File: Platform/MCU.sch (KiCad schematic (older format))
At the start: 28 parts

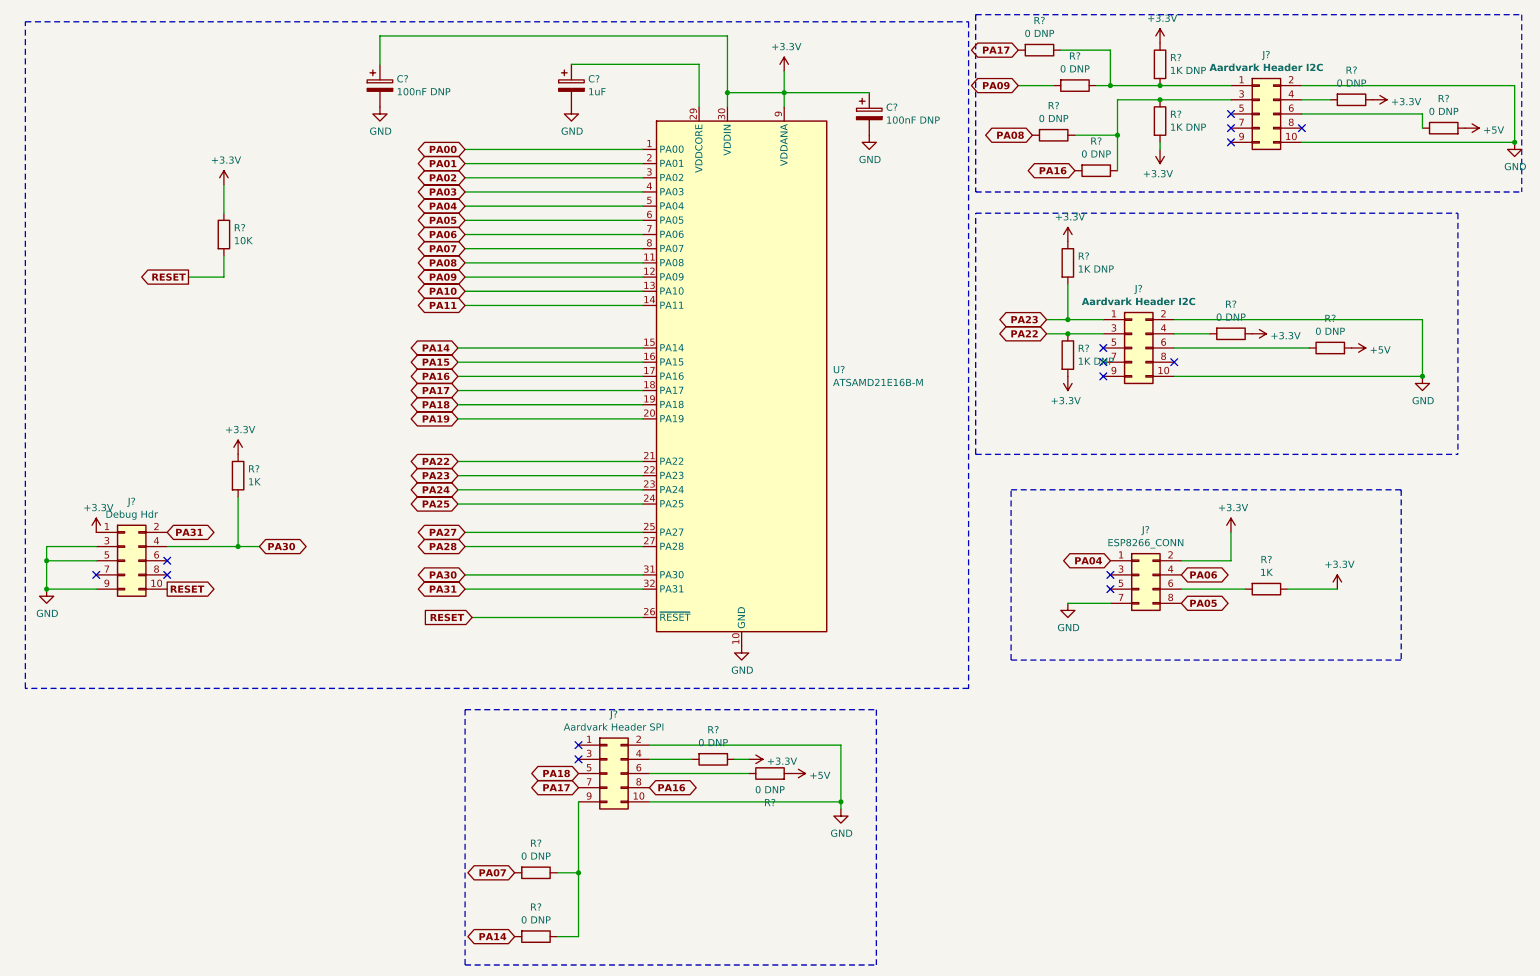
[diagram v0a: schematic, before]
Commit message: Added RTC and EEPROM
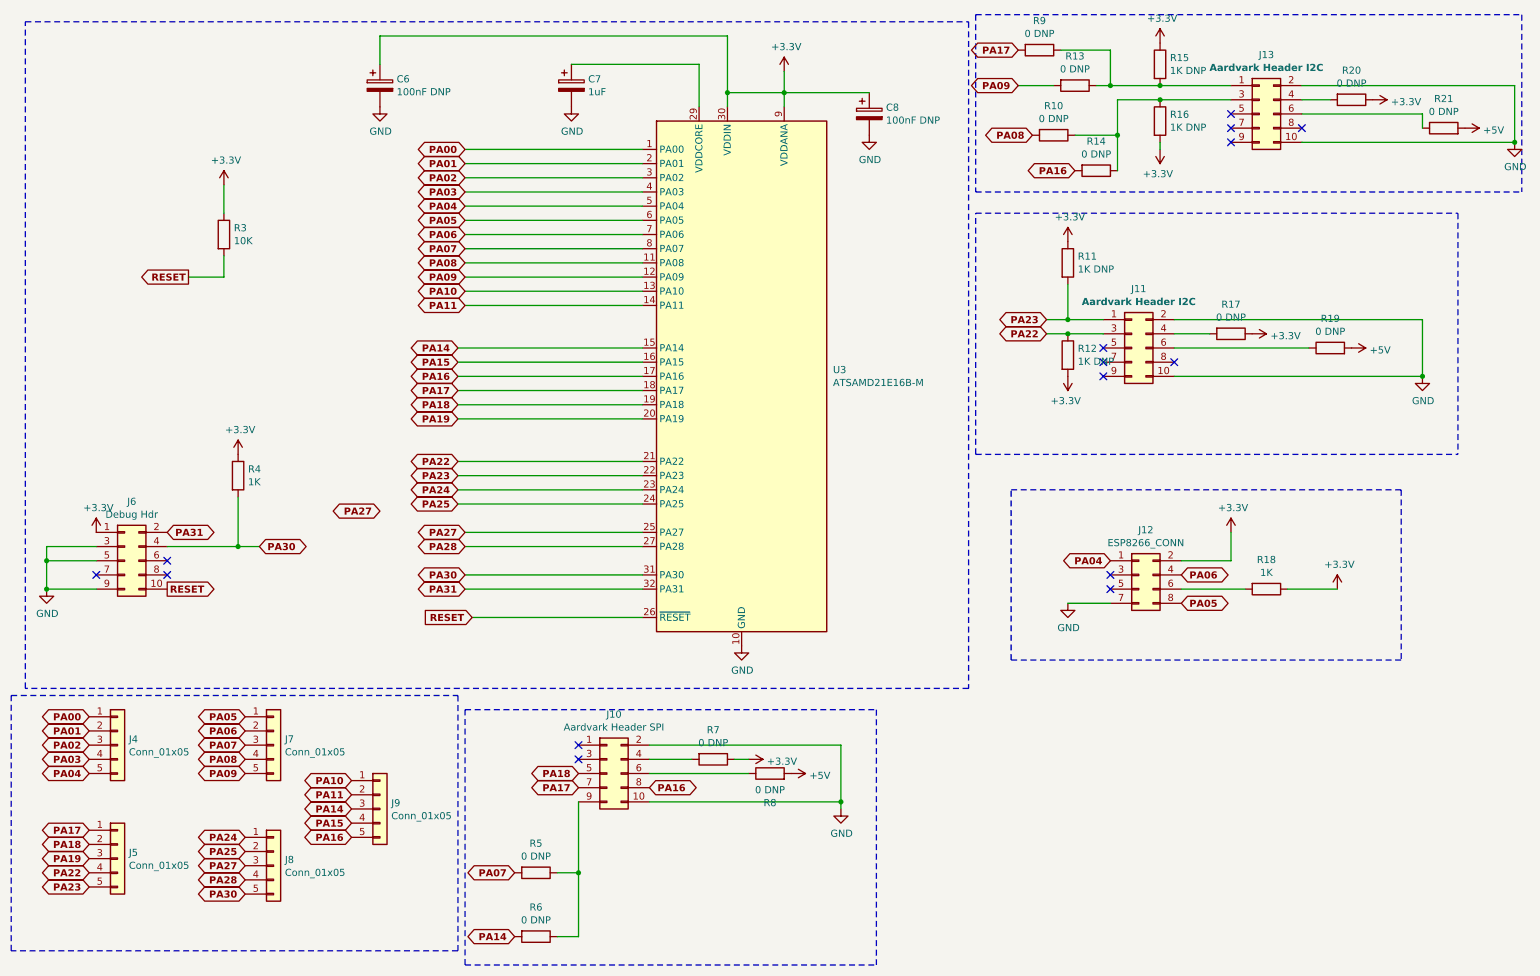
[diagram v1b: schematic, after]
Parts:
- added J4, J5, J7, J8, J9: Conn_01x05, symbol Connector_Generic:Conn_01x05
- gave numbers to parts that had none: 28
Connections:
- net PA00: now also J4.1 (Pin_1)
- net PA01: now also J4.2 (Pin_2)
- net PA02: now also J4.3 (Pin_3)
- net PA03: now also J4.4 (Pin_4)
- net PA04: now also J4.5 (Pin_5)
- net PA05: now also J7.1 (Pin_1)
- net PA06: now also J7.2 (Pin_2)
- net PA07: now also J7.3 (Pin_3)
- net PA08: now also J7.4 (Pin_4)
- net PA09: now also J7.5 (Pin_5)
- net PA10: now also J9.1 (Pin_1)
- net PA11: now also J9.2 (Pin_2)
- net PA14: now also J9.3 (Pin_3)
- net PA15: now also J9.4 (Pin_4)
- net PA16: now also J9.5 (Pin_5)
- net PA17: now also J5.1 (Pin_1)
- net PA18: now also J5.2 (Pin_2)
- net PA19: now also J5.3 (Pin_3)
- net PA22: now also J5.4 (Pin_4)
- net PA23: now also J5.5 (Pin_5)
- net PA24: now also J8.1 (Pin_1)
- net PA25: now also J8.2 (Pin_2)
- net PA27: now also J8.3 (Pin_3)
- net PA28: now also J8.4 (Pin_4)
- net PA30: now also J8.5 (Pin_5)

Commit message: changes
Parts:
- added J9: Conn_01x05, symbol Connector_Generic:Conn_01x05
- renumbered J9 to J10, J10 to J11, J11 to J12, J12 to J13, J13 to J14
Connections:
- net +3V3: now also J9.1 (Pin_1)
- net +5V: now also J9.5 (Pin_5)
- net GND: now also J9.2 (Pin_2), J9.3 (Pin_3), J9.4 (Pin_4)
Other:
- moved on the sheet: J10

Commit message: Fixed ERC errors.
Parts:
- U3: symbol MCU_Microchip_SAMD:ATSAMD21E16B-M -> Platform-rescue:ATSAMD21E16B-M-MCU_Microchip_SAMD
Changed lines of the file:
@@
 RESET
 $Comp
-L MCU_Microchip_SAMD:ATSAMD21E16B-M U3
+L Platform-rescue:ATSAMD21E16B-M-MCU_Microchip_SAMD U3
 U 1 1 5FAA26F4
 P 5700 3450

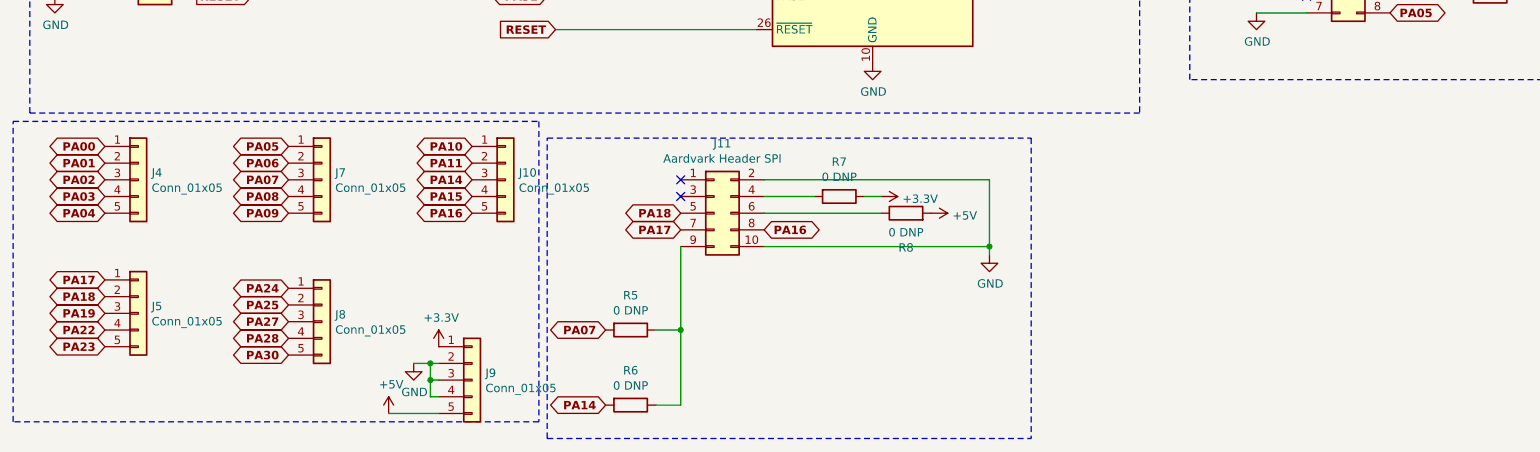
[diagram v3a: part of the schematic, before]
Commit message: added GPIO header for segment display.
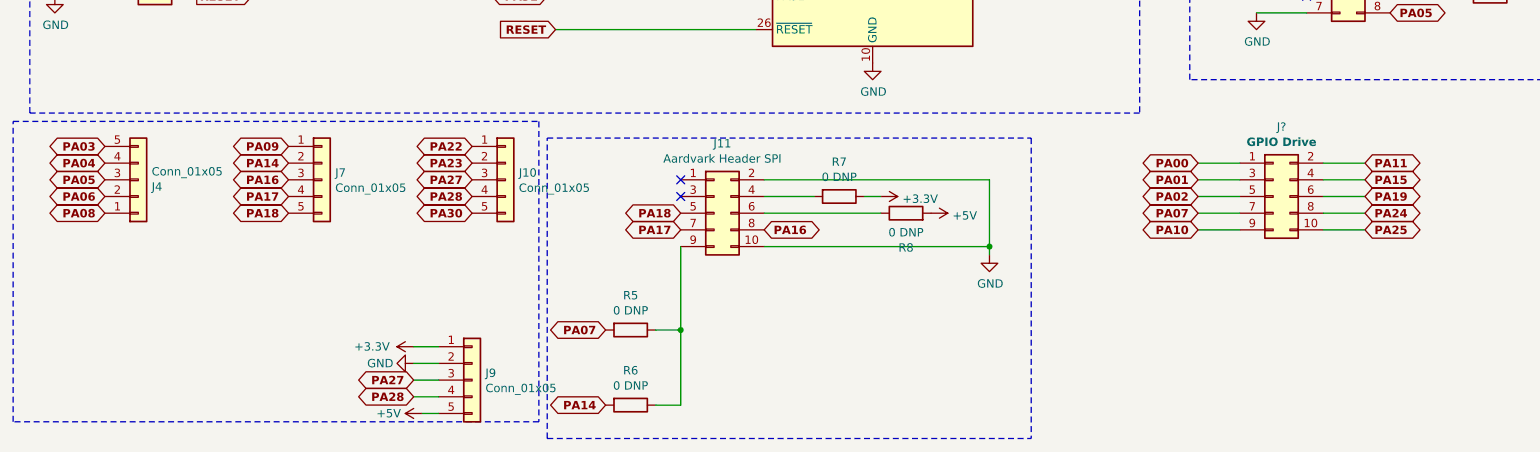
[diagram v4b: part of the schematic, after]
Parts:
- removed J5, J8: Conn_01x05, symbol Connector_Generic:Conn_01x05
- added J?: GPIO Drive, symbol Connector_Generic:Conn_02x05_Odd_Even
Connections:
- net GND: no longer J9.3 (Pin_3), J9.4 (Pin_4)
- net PA00: now also J?.1 (Pin_1); no longer J4.1 (Pin_1)
- net PA01: now also J?.3 (Pin_3); no longer J4.2 (Pin_2)
- net PA02: now also J?.5 (Pin_5); no longer J4.3 (Pin_3)
- net PA03: now also J4.5 (Pin_5); no longer J4.4 (Pin_4)
- net PA04: now also J4.4 (Pin_4); no longer J4.5 (Pin_5)
- net PA05: now also J4.3 (Pin_3); no longer J7.1 (Pin_1)
- net PA06: now also J4.2 (Pin_2); no longer J7.2 (Pin_2)
- net PA07: now also J?.7 (Pin_7); no longer J7.3 (Pin_3)
- net PA08: now also J4.1 (Pin_1); no longer J7.4 (Pin_4)
- net PA09: now also J7.1 (Pin_1); no longer J7.5 (Pin_5)
- net PA10: now also J?.9 (Pin_9); no longer J10.1 (Pin_1)
- net PA11: now also J?.2 (Pin_2); no longer J10.2 (Pin_2)
- net PA14: now also J7.2 (Pin_2); no longer J10.3 (Pin_3)
- net PA15: now also J?.4 (Pin_4); no longer J10.4 (Pin_4)
- net PA16: now also J7.3 (Pin_3); no longer J10.5 (Pin_5)
- net PA17: now also J7.4 (Pin_4)
- net PA18: now also J7.5 (Pin_5)
- net PA19: now also J?.6 (Pin_6)
- net PA22: now also J10.1 (Pin_1)
- net PA23: now also J10.2 (Pin_2)
- net PA24: now also J?.8 (Pin_8)
- net PA25: now also J?.10 (Pin_10)
- net PA27: now also J10.3 (Pin_3), J9.3 (Pin_3)
- net PA28: now also J10.4 (Pin_4), J9.4 (Pin_4)
- net PA30: now also J10.5 (Pin_5)
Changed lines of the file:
@@
 F 3 "~" H 1300 6050 50  0001 C CNN
 	1    1300 6050
-	1    0    0    -1
+	1    0    0    1
 $EndComp
+Text GLabel 7650 5950 0    50   BiDi ~ 10
+PA00
+Text GLabel 7650 6050 0    50   BiDi ~ 10
+PA01
+Text GLabel 7650 6150 0    50   BiDi ~ 10
+PA02
 Text GLabel 1100 5850 0    50   BiDi ~ 10
-PA00
+PA03
 Text GLabel 1100 5950 0    50   BiDi ~ 10
-PA01
-Text GLabel 1100 6050 0    50   BiDi ~ 10
-PA02
-Text GLabel 1100 6150 0    50   BiDi ~ 10
-PA03
-Text GLabel 1100 6250 0    50   BiDi ~ 10
 PA04
 $Comp
@@
 	1    0    0    -1
 $EndComp
-Text GLabel 2200 5850 0    50   BiDi ~ 10
+Text GLabel 1100 6050 0    50   BiDi ~ 10
 PA05
-Text GLabel 2200 5950 0    50   BiDi ~ 10
+Text GLabel 1100 6150 0    50   BiDi ~ 10
 PA06
-Text GLabel 2200 6050 0    50   BiDi ~ 10
+Text GLabel 7650 6250 0    50   BiDi ~ 10
 PA07
-Text GLabel 2200 6150 0    50   BiDi ~ 10
+Text GLabel 1100 6250 0    50   BiDi ~ 10
 PA08
 $Comp
@@
 	1    0    0    -1
 $EndComp
+Text GLabel 7650 6350 0    50   BiDi ~ 10
+PA10
+Text GLabel 8650 5950 2    50   BiDi ~ 10
+PA11
+Text GLabel 2200 5950 0    50   BiDi ~ 10
+PA14
+Text GLabel 8650 6050 2    50   BiDi ~ 10
+PA15
+Text GLabel 2200 6050 0    50   BiDi ~ 10
+PA16
+Text GLabel 2200 6150 0    50   BiDi ~ 10
+PA17
+Text GLabel 2200 6250 0    50   BiDi ~ 10
+PA18
+Text GLabel 8650 6150 2    50   BiDi ~ 10
+PA19
 Text GLabel 3300 5850 0    50   BiDi ~ 10
-PA10
+PA22
 Text GLabel 3300 5950 0    50   BiDi ~ 10
-PA11
+PA23
+Text GLabel 8650 6250 2    50   BiDi ~ 10
+PA24
+Text GLabel 8650 6350 2    50   BiDi ~ 10
+PA25
 Text GLabel 3300 6050 0    50   BiDi ~ 10
-PA14
+PA27
 Text GLabel 3300 6150 0    50   BiDi ~ 10
-PA15
+PA28
 Text GLabel 3300 6250 0    50   BiDi ~ 10
-PA16
-$Comp
-L Connector_Generic:Conn_01x05 J5
-U 1 1 5FB23C68
-P 1300 6850
-F 0 "J5" H 1380 6892 50  0000 L CNN
-F 1 "Conn_01x05" H 1380 6801 50  0000 L CNN
-F 2 "" H 1300 6850 50  0001 C CNN
-F 3 "~" H 1300 6850 50  0001 C CNN
-	1    1300 6850
-	1    0    0    -1
-$EndComp
-Text GLabel 1100 6650 0    50   BiDi ~ 10
-PA17
-Text GLabel 1100 6750 0    50   BiDi ~ 10
-PA18
-Text GLabel 1100 6850 0    50   BiDi ~ 10
-PA19
-Text GLabel 1100 6950 0    50   BiDi ~ 10
-PA22
-Text GLabel 1100 7050 0    50   BiDi ~ 10
-PA23
-$Comp
-L Connector_Generic:Conn_01x05 J8
-U 1 1 5FB26618
-P 2400 6900
-F 0 "J8" H 2480 6942 50  0000 L CNN
-F 1 "Conn_01x05" H 2480 6851 50  0000 L CNN
-F 2 "" H 2400 6900 50  0001 C CNN
-F 3 "~" H 2400 6900 50  0001 C CNN
-	1    2400 6900
-	1    0    0    -1
-$EndComp
-Text GLabel 2200 6700 0    50   BiDi ~ 10
-PA24
-Text GLabel 2200 6800 0    50   BiDi ~ 10
-PA25
-Text GLabel 2200 6900 0    50   BiDi ~ 10
-PA27
-Text GLabel 2200 7000 0    50   BiDi ~ 10
-PA28
-Text GLabel 2200 7100 0    50   BiDi ~ 10
 PA30
-Text GLabel 2200 6250 0    50   BiDi ~ 10
+Text GLabel 2200 5850 0    50   BiDi ~ 10
 PA09
 Wire Notes Line
@@
 L power:+3.3V #PWR019
 U 1 1 5FB2EBC0
-P 3100 7050
-F 0 "#PWR019" H 3100 6900 50  0001 C CNN
-F 1 "+3.3V" H 3115 7223 50  0000 C CNN
-F 2 "" H 3100 7050 50  0001 C CNN
-F 3 "" H 3100 7050 50  0001 C CNN
-	1    3100 7050
-	1    0    0    -1
+P 2950 7050
+F 0 "#PWR019" H 2950 6900 50  0001 C CNN
+F 1 "+3.3V" V 2950 7300 50  0000 C CNN
+F 2 "" H 2950 7050 50  0001 C CNN
+F 3 "" H 2950 7050 50  0001 C CNN
+	1    2950 7050
+	0    -1   -1   0
 $EndComp
 $Comp
 L power:+5V #PWR017
 U 1 1 5FB2F62B
-P 2800 7450
-F 0 "#PWR017" H 2800 7300 50  0001 C CNN
-F 1 "+5V" H 2815 7623 50  0000 C CNN
-F 2 "" H 2800 7450 50  0001 C CNN
-F 3 "" H 2800 7450 50  0001 C CNN
-	1    2800 7450
-	1    0    0    -1
+P 3000 7450
+F 0 "#PWR017" H 3000 7300 50  0001 C CNN
+F 1 "+5V" V 3000 7650 50  0000 C CNN
+F 2 "" H 3000 7450 50  0001 C CNN
+F 3 "" H 3000 7450 50  0001 C CNN
+	1    3000 7450
+	0    -1   -1   0
 $EndComp
 Wire Wire Line
-	2800 7450 3100 7450
+	3000 7450 3100 7450
 $Comp
 L power:GND #PWR018
@@
 P 2950 7150
 F 0 "#PWR018" H 2950 6900 50  0001 C CNN
-F 1 "GND" H 2955 6977 50  0000 C CNN
+F 1 "GND" V 2950 6950 50  0000 C CNN
 F 2 "" H 2950 7150 50  0001 C CNN
 F 3 "" H 2950 7150 50  0001 C CNN
 	1    2950 7150
+	0    1    1    0
+$EndComp
+Wire Wire Line
+	2950 7150 3100 7150
+Wire Wire Line
+	2950 7050 3100 7050
+Text GLabel 2950 7250 0    50   BiDi ~ 10
+PA27
+Text GLabel 2950 7350 0    50   BiDi ~ 10
+PA28
+Wire Wire Line
+	2950 7250 3100 7250
+Wire Wire Line
+	2950 7350 3100 7350
+$Comp
+L Connector_Generic:Conn_02x05_Odd_Even J?
+U 1 1 5FBB860D
+P 8100 6150
+F 0 "J?" H 8150 6567 50  0000 C CNN
+F 1 "GPIO Drive" H 8150 6476 50  0000 C CNB
+F 2 "" H 8100 6150 50  0001 C CNN
+F 3 "~" H 8100 6150 50  0001 C CNN
+	1    8100 6150
 	1    0    0    -1
 $EndComp
 Wire Wire Line
-	2950 7150 3050 7150
+	7650 5950 7900 5950
 Wire Wire Line
-	3050 7350 3100 7350
+	7900 6050 7650 6050
 Wire Wire Line
-	3050 7350 3050 7250
-Connection ~ 3050 7150
+	7650 6150 7900 6150
 Wire Wire Line
-	3050 7150 3100 7150
+	7900 6250 7650 6250
 Wire Wire Line
-	3100 7250 3050 7250
-Connection ~ 3050 7250
+	7650 6350 7900 6350
 Wire Wire Line
-	3050 7250 3050 7150
+	8400 6350 8650 6350
+Wire Wire Line
+	8650 6250 8400 6250
+Wire Wire Line
+	8400 6150 8650 6150
+Wire Wire Line
+	8650 6050 8400 6050
+Wire Wire Line
+	8400 5950 8650 5950
 $EndSCHEMATC

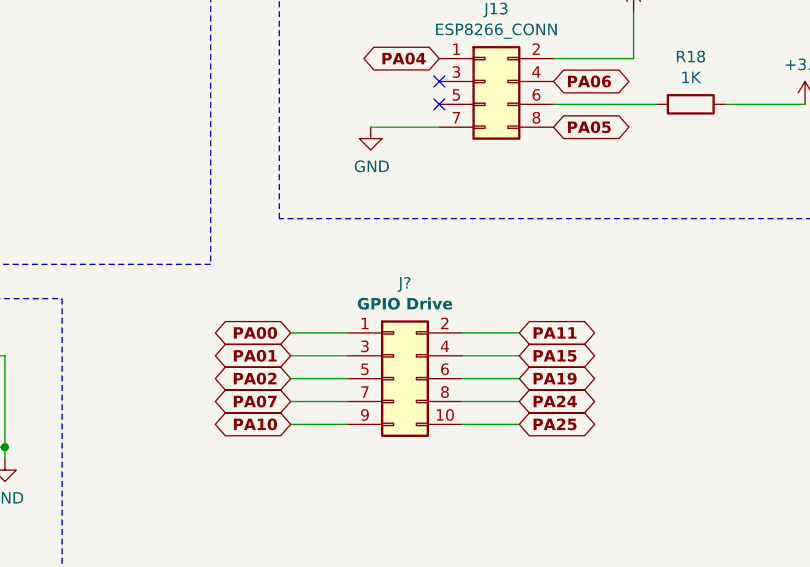
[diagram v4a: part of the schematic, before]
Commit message: updated the crystal and cleared ERC errors.
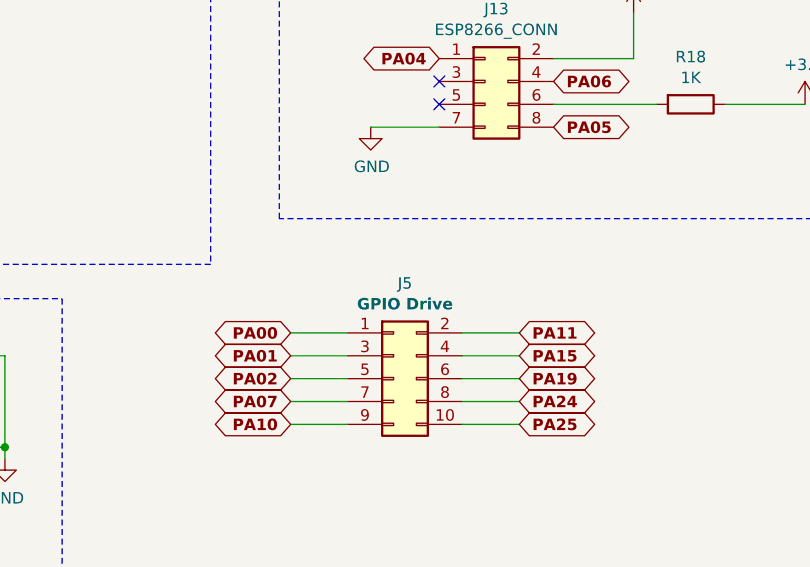
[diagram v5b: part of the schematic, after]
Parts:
- gave numbers to parts that had none: 1
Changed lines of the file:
@@
 	2950 7350 3100 7350
 $Comp
-L Connector_Generic:Conn_02x05_Odd_Even J?
+L Connector_Generic:Conn_02x05_Odd_Even J5
 U 1 1 5FBB860D
 P 8100 6150
-F 0 "J?" H 8150 6567 50  0000 C CNN
+F 0 "J5" H 8150 6567 50  0000 C CNN
 F 1 "GPIO Drive" H 8150 6476 50  0000 C CNB
 F 2 "" H 8100 6150 50  0001 C CNN

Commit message: updated.
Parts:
- U3: symbol Platform-rescue:ATSAMD21E16B-M-MCU_Microchip_SAMD -> Platform-rescue:ATSAMD21E16B-M-MCU_Microchip_SAMD-Platform-rescue
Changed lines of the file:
@@
 RESET
 $Comp
-L Platform-rescue:ATSAMD21E16B-M-MCU_Microchip_SAMD U3
+L Platform-rescue:ATSAMD21E16B-M-MCU_Microchip_SAMD-Platform-rescue U3
 U 1 1 5FAA26F4
 P 5700 3450
+AR Path="/5FAA26F4" Ref="U3"  Part="1"
+AR Path="/5FB6B44D/5FAA26F4" Ref="U3"  Part="1"
 F 0 "U3" H 6344 3496 50  0000 L CNN
 F 1 "ATSAMD21E16B-M" H 6344 3405 50  0000 L CNN

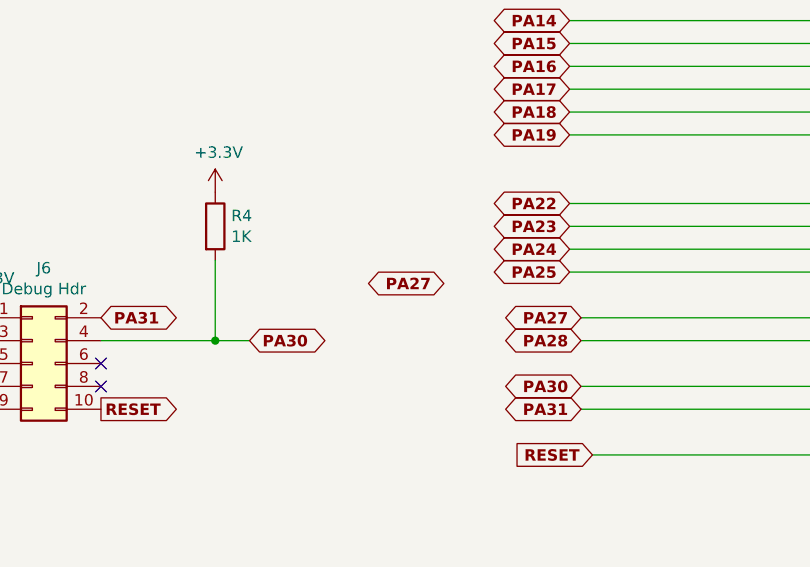
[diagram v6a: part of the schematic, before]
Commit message: Added foot prints for the components.
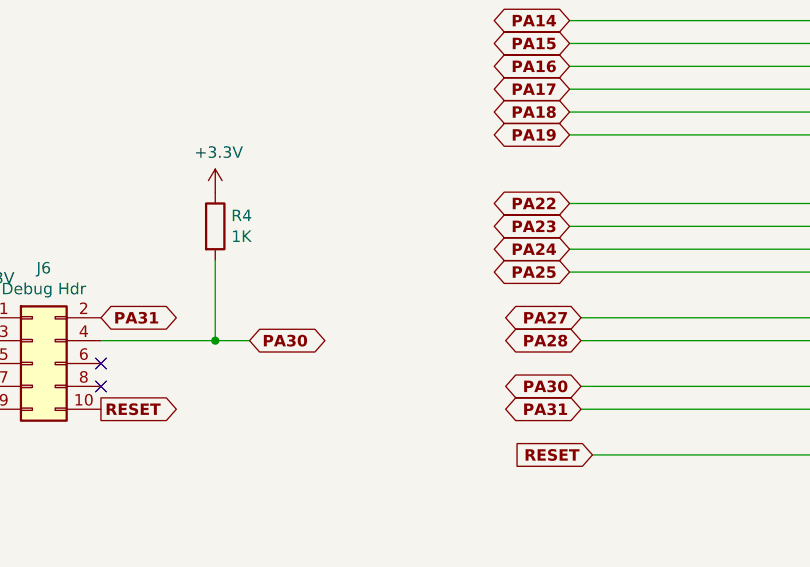
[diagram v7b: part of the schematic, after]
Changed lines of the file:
@@
 Wire Notes Line
 	550  7500 550  5700
-Text GLabel 3150 4400 0    50   BiDi ~ 10
-PA27
 $Comp
 L Connector_Generic:Conn_01x05 J9
